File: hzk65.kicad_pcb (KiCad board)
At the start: 2 copper layers, 314.3 x 100 mm, 135 parts, among them SW1 SW_Push, SW10 SW_Push, SW11 SW_Push, SW12 SW_Push, SW13 SW_Push, SW14 SW_Push, SW16 SW_Push, SW17 SW_Push, SW18 SW_Push, SW19 SW_Push, SW2 SW_Push, SW20 SW_Push, SW21 SW_Push, SW22 SW_Push, SW23 SW_Push, SW24 SW_Push, SW25 SW_Push, SW26 SW_Push, SW27 SW_Push, SW28 SW_Push, SW29 SW_Push, SW3 SW_Push, SW31 SW_Push, SW32 SW_Push, SW33 SW_Push, SW34 SW_Push, SW35 SW_Push, SW36 SW_Push, SW37 SW_Push, SW38 SW_Push, SW39 SW_Push, SW4 SW_Push, SW40 SW_Push, SW41 SW_Push, SW42 SW_Push, SW44 SW_Push, SW46 SW_Push, SW48 SW_Push, SW49 SW_Push, SW5 SW_Push, SW50 SW_Push, SW51 SW_Push, SW52 SW_Push, SW53 SW_Push, SW54 SW_Push, SW55 SW_Push, SW56 SW_Push, SW57 SW_Push, SW58 SW_Push, SW59 SW_Push, SW6 SW_Push, SW60 SW_Push, SW61 SW_Push, SW62 SW_Push, SW63 SW_Push, SW67 SW_Push, SW7 SW_Push, SW70 SW_Push, SW71 SW_Push, SW72 SW_Push, SW73 SW_Push, SW74 SW_Push, SW75 SW_Push, SW8 SW_Push, SW9 SW_Push

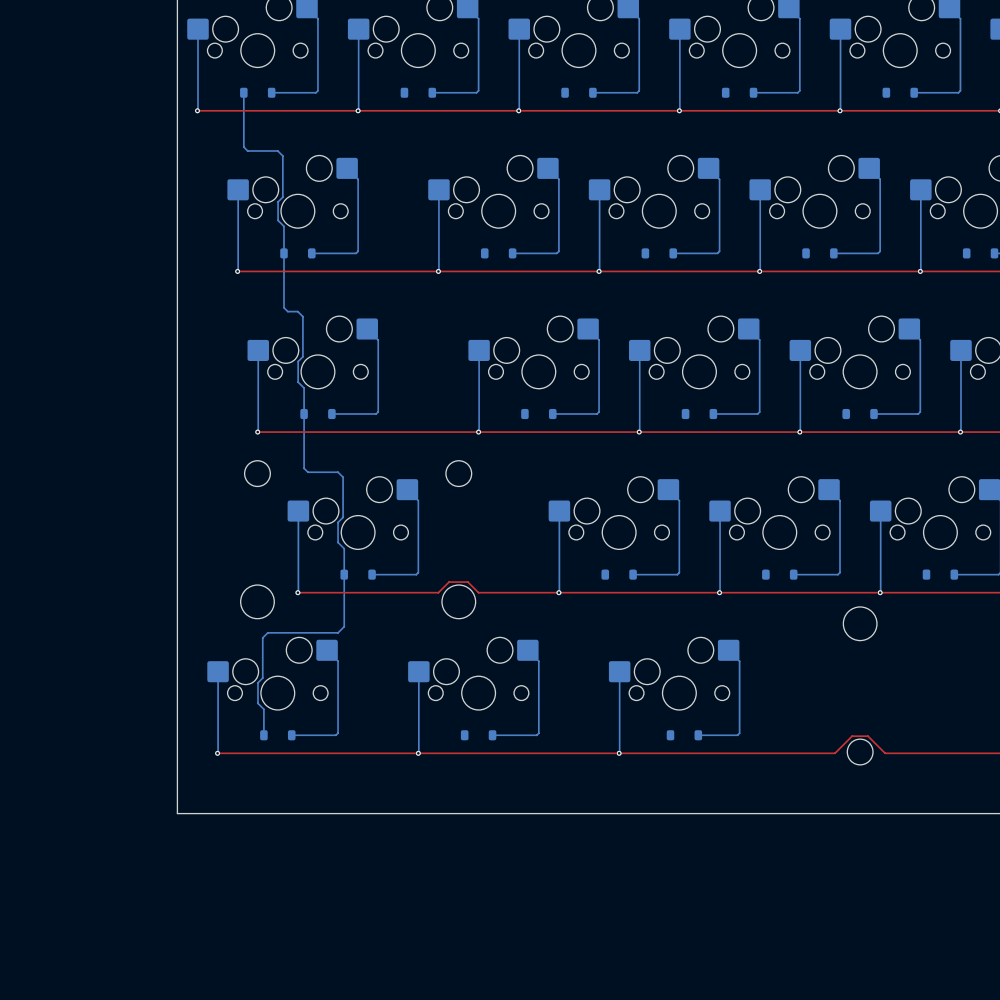
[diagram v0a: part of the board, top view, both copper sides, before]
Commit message: Add logo silkscreens
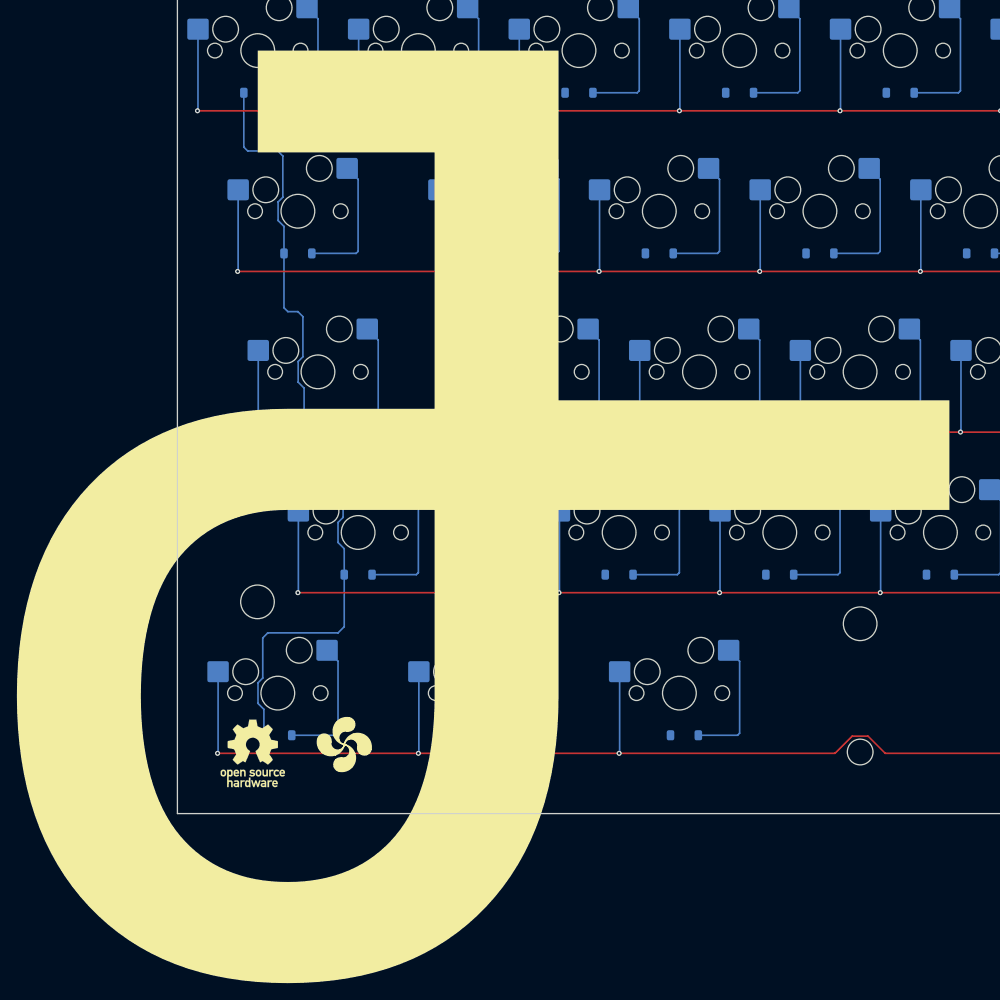
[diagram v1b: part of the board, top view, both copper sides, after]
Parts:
- added REF**: OSHW-Logo_7.5x8mm_SilkScreen, Symbol:OSHW-Logo_7.5x8mm_SilkScreen, F.Cu at (61.3, 192.9)

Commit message: Add oshw logo reference
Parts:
- renumbered REF** to L1
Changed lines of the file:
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@@
 		(descr "Open Source Hardware Logo")
 		(tags "Logo OSHW")
-		(property "Reference" "REF**"
+		(property "Reference" "L1"
 			(at 0 0 0)
 			(layer "F.SilkS")

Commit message: Fix drc via and silkscreen warnings
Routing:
- net /ROW1: vias 15 -> 14
- net /ROW0: vias 15 -> 14
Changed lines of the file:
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@@
-	)
-	(via
-		(at 283.3747 116.681348)
-		(size 0.6)
-		(drill 0.3)
-		(layers "F.Cu" "B.Cu")
-		(net "/ROW0")
 	)
 	(via
@@
 		(size 0.6)
 		(drill 0.3)
-		(layers "F.Cu" "B.Cu")
-		(net "/ROW1")
-	)
-	(via
-		(at 292.8999 135.731364)
-		(size 0.6)
-		(drill 0.3)

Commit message: Route all switches
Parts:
- moved D63 0.60 mm to (111.9, 190.7)
- renumbered L1 to GL1, S14 to H14, S44 to H44, S46 to H46, S67 to H67
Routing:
- net /COL11: track 0.00 -> 113.5 mm
- net /COL9: track 0.00 -> 113.5 mm
- net /COL10: track 0.00 -> 113.5 mm
- net /COL13: track 0.00 -> 109.7 mm
- net /COL2: track 0.00 -> 106.3 mm
- net /COL12: track 0.00 -> 104.1 mm
- net /COL6: track 0.00 -> 101.6 mm
- net /COL1: track 0.00 -> 96.4 mm
- net /COL3: track 0.00 -> 80.4 mm
- net /COL4: track 0.00 -> 80.4 mm
- net /COL5: track 0.00 -> 80.4 mm
- net /COL7: track 0.00 -> 80.4 mm
- net /COL8: track 0.00 -> 80.4 mm
- net /ROW0: track 394.1 -> 362.9 mm
- net /ROW1: track 393.1 -> 362.9 mm
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
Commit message: Add copper pours
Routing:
- added copper zone on B.Cu, net GND
- added copper zone on F.Cu, net GND
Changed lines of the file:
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@@
 		(capping no)
 		(filling no)
-		(zone_defaults)
 		(grid_origin 52.3886 100.0146)
 		(pcbplotparams
@@
 		)
 		(fp_line
-			(start 12.49 49.74)
-			(end 5.29 49.74)
-			(stroke
-				(width 0.12)
-				(type solid)
-			)
-			(layer "B.SilkS")
-		)
-		(fp_line
 			(start 13.125 -1.48)
 			(end 14.127939 -1.48)
@@
 		)
 		(fp_arc
-			(start -1.11 49.74)
-			(mid -1.541364 49.561364)
-			(end -1.72 49.13)
-			(stroke
-				(width 0.12)
-				(type solid)
-			)
-			(layer "B.SilkS")
-		)
-		(fp_arc
 			(start 18.89 -1.48)
 			(mid 19.321335 -1.301335)
@@
 			(layer "B.SilkS")
 		)
-		(fp_arc
-			(start 19.5 49.13)
-			(mid 19.321335 49.561335)
-			(end 18.89 49.74)
-			(stroke
-				(width 0.12)
-				(type solid)
-			)
-			(layer "B.SilkS")
-		)
 		(fp_circle
 			(center 3.19 0.63)
@@
 			)
 		)
-		(fp_text user "Possible Antenna"
-			(at 8.89 43.815 0)
-			(unlocked yes)
-			(layer "Cmts.User")
-			(effects
-				(font
-					(size 1 1)
-					(thickness 0.15)
-				)
-			)
-		)
-		(fp_text user "Keep Out"
-			(at 8.89 45.72 0)
-			(unlocked yes)
-			(layer "Cmts.User")
-			(effects
-				(font
-					(size 1 1)
-					(thickness 0.15)
-				)
-			)
-		)
 		(fp_text user "${REFERENCE}"
 			(at 8.89 24.13 90)
@@
 		)
 		(zone
-			(layers "F.Cu" "B.Cu" "F.Paste" "B.Paste")
-			(name "Antenna Copper Keep Out")
-			(hatch full 0.5)
-			(connect_pads
-				(clearance 0)
-			)
-			(min_thickness 0.254)
-			(keepout
-				(tracks not_allowed)
-				(vias not_allowed)
-				(pads not_allowed)
-				(copperpour not_allowed)
-				(footprints allowed)
-			)
-			(placement
-				(enabled no)
-				(sheetname "")
-			)
-			(fill
-				(thermal_gap 0.508)
-				(thermal_bridge_width 0.508)
-				(island_removal_mode 0)
-			)
-			(polygon
-				(pts
-					(xy 352.4124 151.200145) (xy 347.7124 147.550145) (xy 347.7124 143.21025) (xy 361.9124 143.21025)
-					(xy 361.9124 147.550145) (xy 357.2124 151.200145) (xy 357.2124 152.21025) (xy 352.4124 152.21025)
-				)
-			)
-		)
-		(zone
 			(layer "F.CrtYd")
 			(name "USB Cable")
@@
 		)
 		(group ""
-			(members "2e304350-e30e-4e39-ba45-6ac520590cfe" "5c963364-9bb5-42bc-a8b4-08978afe9b04"
-				"7403b13a-43d1-4d03-88a0-d4543067d90b" "91a12ac4-8ebd-4743-8fab-b0fd9812f8c8"
-				"f41baa4a-8270-4458-a1cd-b3bf137133a7" "fa379e11-87f0-46c8-b8bb-95f9f62df58e"
-			)
-		)
-		(group ""
 			(members "0f8aa358-31f5-4c84-95fd-80b596f979e4" "623f9920-48af-4773-83e8-58070bc1f2ba"
 				"6826fa9e-08ea-4b45-8d48-58fab47cc32b" "871f2ecb-2d65-4ab8-af53-8ce1d5f86def"
@@
 		(net "Net-(D70-A)")
 	)
+	(zone
+		(net "GND")
+		(layer "F.Cu")
+		(hatch edge 0.5)
+		(priority 1)
+		(connect_pads
+			(clearance 0.5)
+		)
+		(min_thickness 0.25)
+		(fill yes
+			(thermal_gap 0.5)
+			(thermal_bridge_width 0.5)
+			(island_removal_mode 1)
+		)
+		(polygon
+			(pts
+				(xy 52.3873 100.0146) (xy 366.707 100.0146) (xy 366.707 200.025) (xy 52.3886 200.025)
+			)
+		)
+	)
+	(zone
+		(net "GND")
+		(layer "B.Cu")
+		(hatch edge 0.5)
+		(connect_pads
+			(clearance 0.5)
+		)
+		(min_thickness 0.25)
+		(fill yes
+			(thermal_gap 0.5)
+			(thermal_bridge_width 0.5)
+			(island_removal_mode 1)
+		)
+		(polygon
+			(pts
+				(xy 52.3886 100.0146) (xy 366.707 100.0146) (xy 366.707 200.025) (xy 52.3886 200.025)
+			)
+		)
+	)
 	(embedded_fonts no)

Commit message: Add stitching vias
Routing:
- net Net-(D75-A): vias 0 -> 1
- net GND: vias 0 -> 45
- net /COL9: vias 0 -> 3
- net /COL8: vias 0 -> 2
- net /COL7: vias 0 -> 2
- net /COL6: vias 0 -> 2
- net /COL5: vias 0 -> 2
- net /COL4: vias 0 -> 2
- net /COL3: vias 0 -> 2
- net /COL2: vias 0 -> 3
- net /COL13: vias 0 -> 2
- net /COL12: vias 0 -> 1
- net /COL11: vias 0 -> 3
- net /COL10: vias 0 -> 3
- net /COL1: vias 0 -> 2
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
